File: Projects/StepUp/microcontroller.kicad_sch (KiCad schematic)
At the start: 31 parts, among them J1 USB_C_Receptacle_USB2.0_16P, J3 Conn_02x03_Odd_Even, J4 Conn_02x06_Odd_Even, SW1 PTS636SL43SMTRLFS, SW5 PTS636SL43SMTRLFS, U1 USBLC6-2SC6, U10 W25Q16JVUXIQ TR, U3 RP2040, Y1 ABM8-272-T3

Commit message: feat(v0.2): Rough layout begins
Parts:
- removed J4: Conn_02x06_Odd_Even, Connector_PinHeader_2.54mm:PinHeader_2x06_P2.54mm_Vertical, symbol Connector_Generic:Conn_02x06_Odd_Even
- removed SW5: PTS636SL43SMTRLFS, Snapeda:SW_PTS636S-J_CNK, symbol Snapeda_kicad:PTS636SL43SMTRLFS
- added SW2: PTS636SL43SMTRLFS, Snapeda:SW_PTS636S-J_CNK, symbol Snapeda_kicad:PTS636SL43SMTRLFS
- D1: Description_1 (none) -> DIODE GEN PURP 100V 150MA SOD123; Digi-Key_PN (none) -> 1N4148WTPMSCT-ND
- renumbered C15 to C14, J3 to J2, U10 to U1, U1 to U2
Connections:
- net GND: now also SW2.1
- net RUN: now also SW1.2
- net at D1.K: now also SW2.2; no longer SW1.2
- no-connect marks 2 -> 9
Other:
- note added: "Run - resets MCU USB_BOOT - hold this and toggle Run to enumerate as USB device for UF2 firmware upload NOTE: Buttons are SMD and usually hidden from user"
- note removed: "I2C_0/1 SPI_1 UART_0"
- note removed: "I2C_1"
- note removed: "Run - resets MCU USB_BOOT - hold this and toggle Run to enumerate as USB device for UF2 firmware upload"

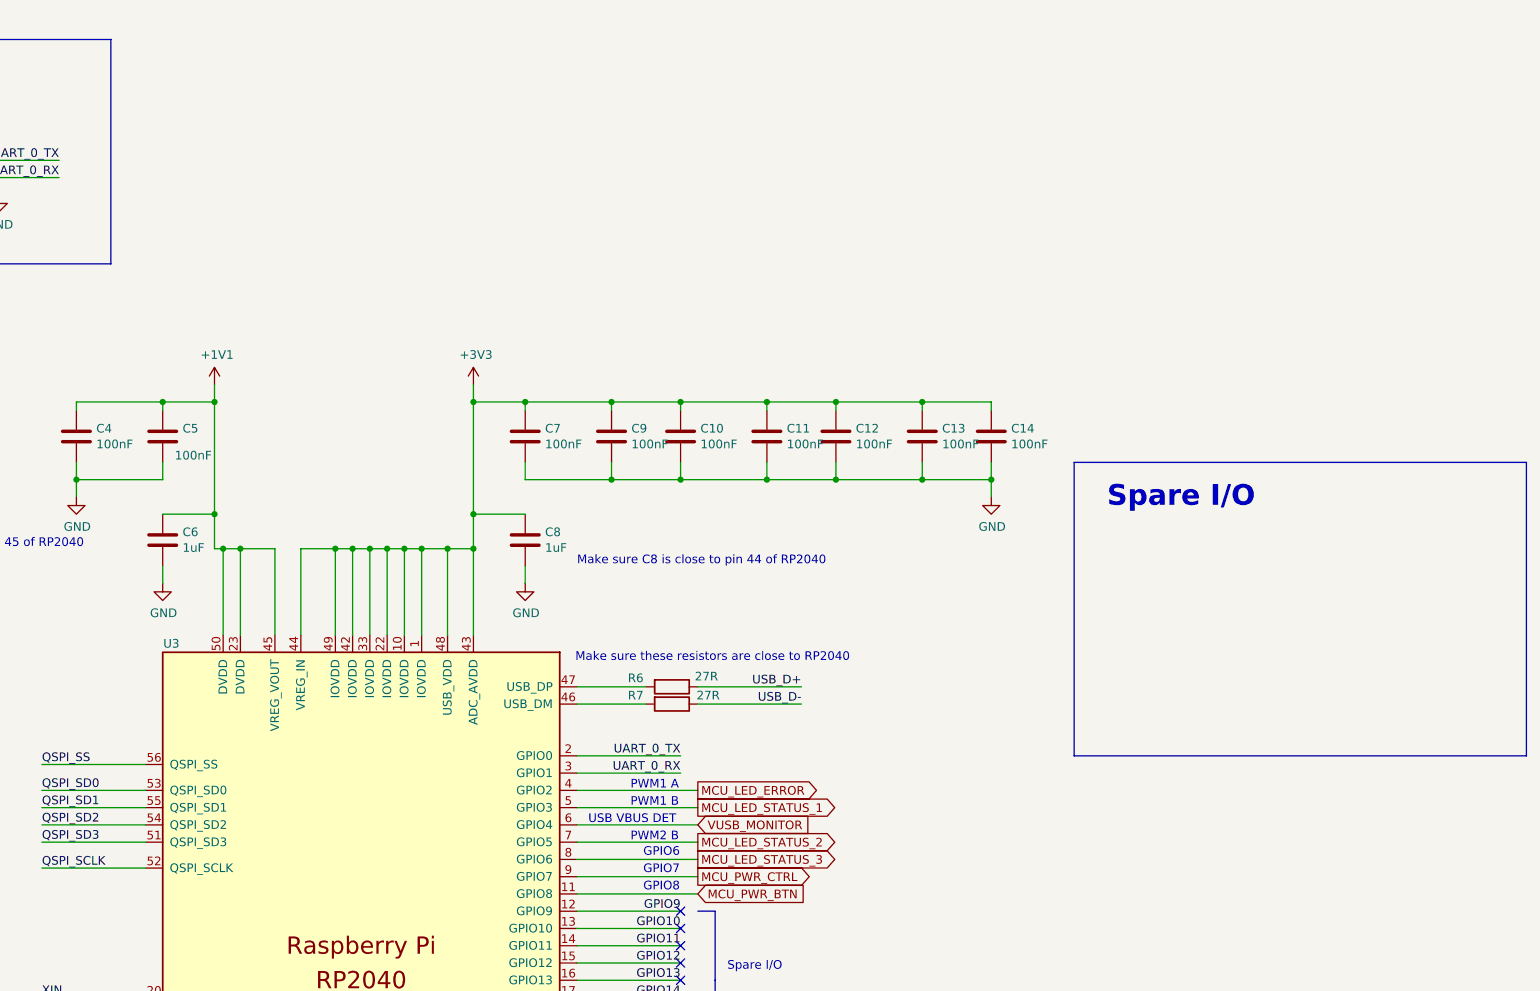
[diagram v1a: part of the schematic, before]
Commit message: feat(v0.2): Component layout from CAD
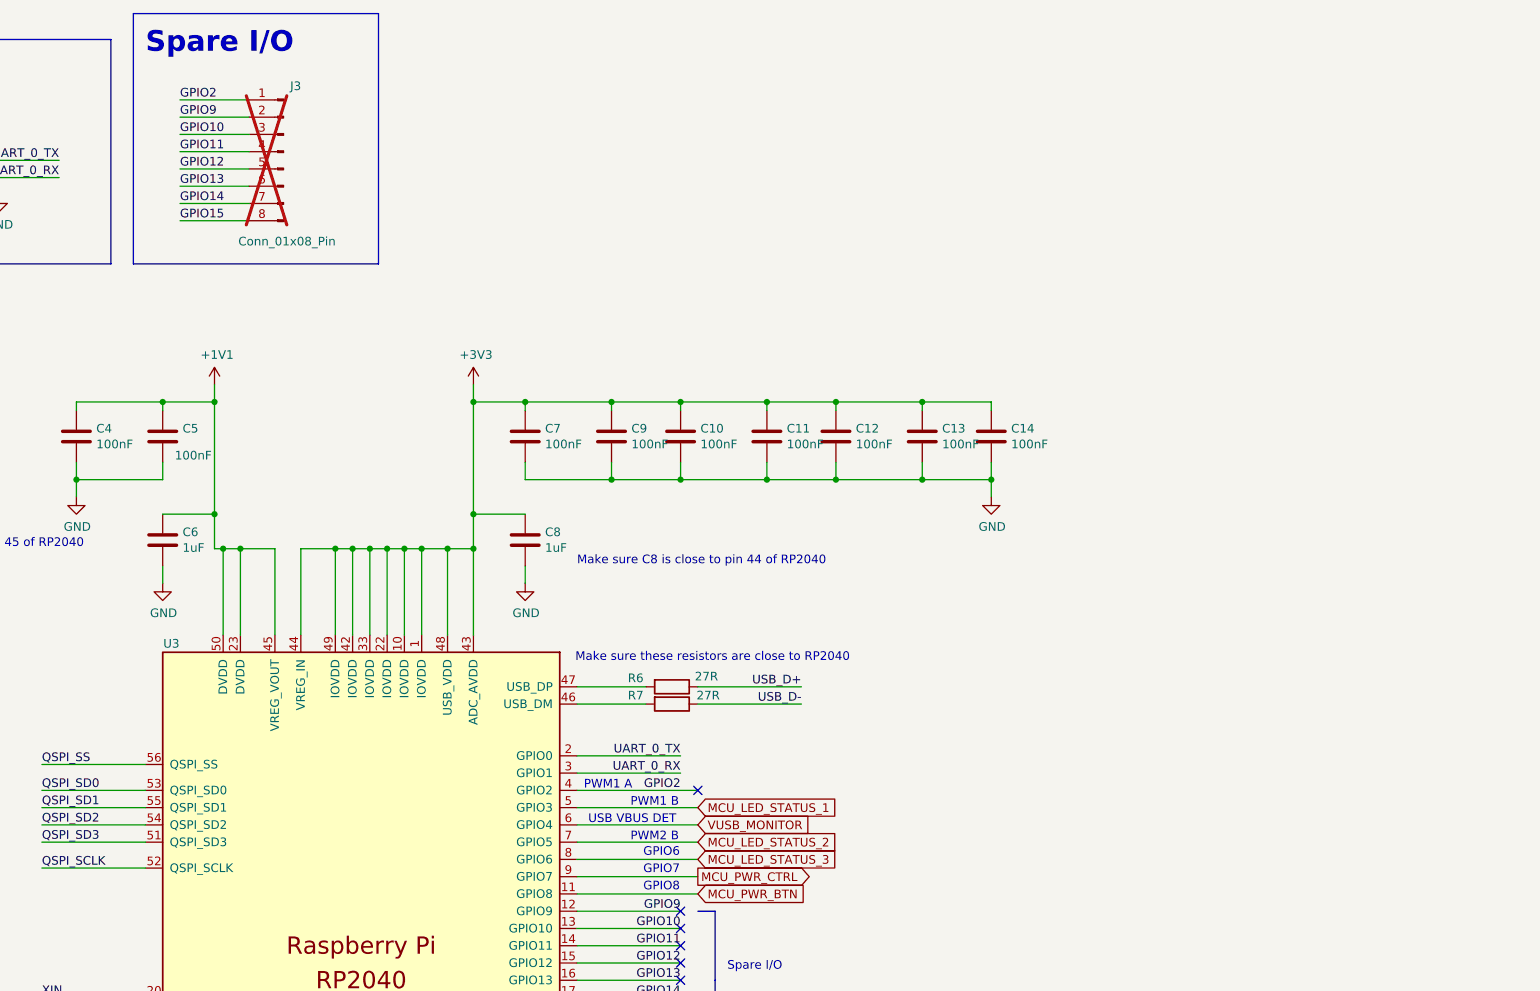
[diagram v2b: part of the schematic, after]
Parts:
- added J3: Conn_01x08_Pin, Connector_PinHeader_2.54mm:PinHeader_1x08_P2.54mm_Vertical, symbol Connector:Conn_01x08_Pin
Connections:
- net GPIO10: now also J3.3 (Pin_3)
- net GPIO11: now also J3.4 (Pin_4)
- net GPIO12: now also J3.5 (Pin_5)
- net GPIO13: now also J3.6 (Pin_6)
- net GPIO14: now also J3.7 (Pin_7)
- net GPIO15: now also J3.8 (Pin_8)
- net GPIO9: now also J3.2 (Pin_2)
- net MCU_LED_ERROR renamed GPIO2
- net GPIO2: now also J3.1 (Pin_1)
- no-connect marks 9 -> 10

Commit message: feat(v0.2): Release, PCBs ordered!
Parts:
- removed J3: Conn_01x08_Pin, Connector_PinHeader_2.54mm:PinHeader_1x08_P2.54mm_Vertical, symbol Connector:Conn_01x08_Pin
- added J5: Conn_01x09_Pin, Connector_PinHeader_2.54mm:PinHeader_1x09_P2.54mm_Vertical, symbol Connector:Conn_01x09_Pin
- J2: now fitted; now left out of the parts list
- SW1, SW2: value PTS636SL43SMTRLFS -> PTS636SP43SMTRL FS; MPN (none) -> PTS636SP43SMTR LFS; Manufacturer (none) -> C&K
- U1: MPN (none) -> W25Q16JVUXIQ TR; Manufacturer (none) -> Winbond Electronics
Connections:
- net GND: now also J5.1 (Pin_1)
- net GPIO10: now also J5.4 (Pin_4)
- net GPIO11: now also J5.5 (Pin_5)
- net GPIO12: now also J5.6 (Pin_6)
- net GPIO13: now also J5.7 (Pin_7)
- net GPIO14: now also J5.8 (Pin_8)
- net GPIO15: now also J5.9 (Pin_9)
- net GPIO2: now also J5.2 (Pin_2)
- net GPIO9: now also J5.3 (Pin_3)
- no-connect marks 10 -> 2

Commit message: feat(v0.3): Begin work on next rev
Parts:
- renumbered J5 to J2, J2 to J3
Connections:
- net MCU_LED_STATUS_1 renamed MCU_LED_RED
- net MCU_LED_STATUS_2 renamed MCU_LED_BLUE
- net MCU_LED_STATUS_3 renamed MCU_LED_GREEN

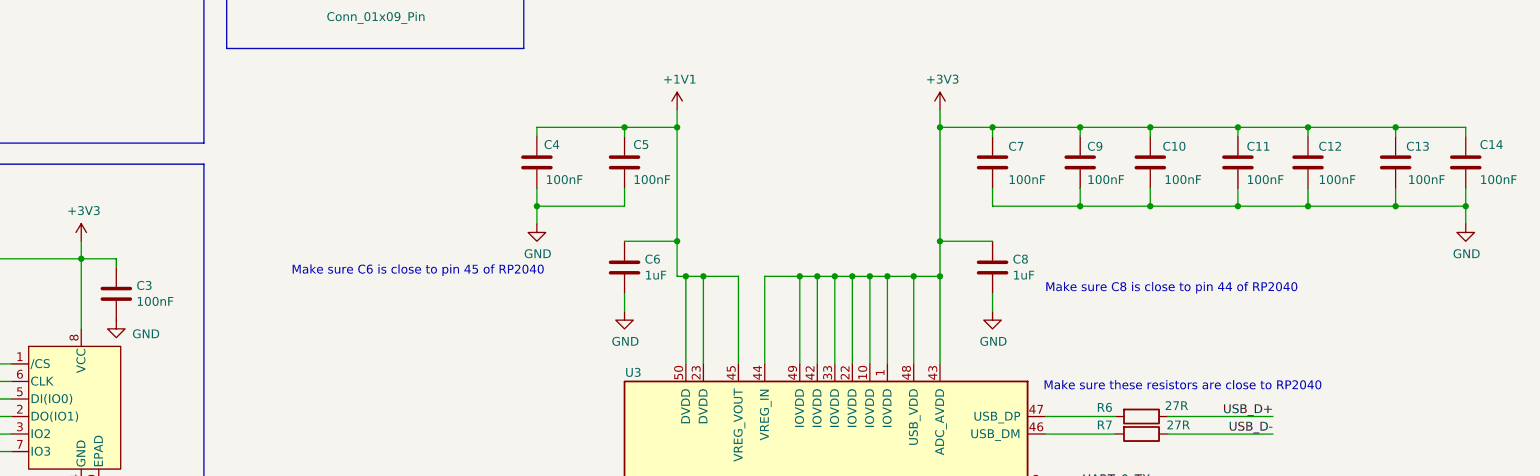
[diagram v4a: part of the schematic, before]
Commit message: feat(v0.3): Boost layout complete
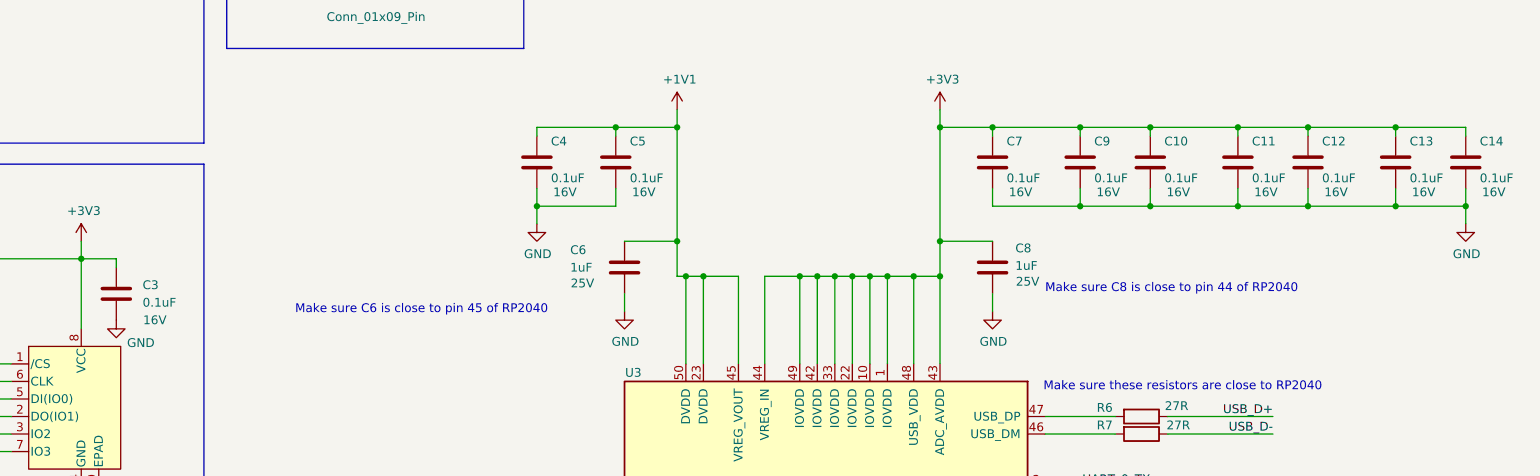
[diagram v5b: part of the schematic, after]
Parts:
- C10, C11, C12, C13, C14, C3, C4, C5, C7, C9: value 100nF -> 0.1uF; Dielectric X7R -> X5R; MPN CC0402KRX7R8BB104 -> GRM155R61C104KA88D; Manufacturer YAGEO -> Murata; Package 0402 -> 0402; Voltage 25V -> 16V
- C6, C8: footprint Capacitor_SMD:C_0402_1005Metric -> Capacitor_SMD:C_0603_1608Metric; Dielectric X5R -> X7R; MPN GRM155R61E105MA12D -> GRM188R71E105KA12D; Manufacturer Murata Electronics -> Murata; Package 0402 -> 0603; Tolerance 20% -> 10%

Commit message: feat(v0.3): Layout 90% complete
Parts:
- removed J2: Conn_01x09_Pin, Connector_PinHeader_2.54mm:PinHeader_1x09_P2.54mm_Vertical, symbol Connector:Conn_01x09_Pin
- removed SW1, SW2: PTS636SP43SMTRL FS, Snapeda:SW_PTS636S-J_CNK, symbol Snapeda_kicad:PTS636SL43SMTRLFS
- added J2: Conn_01x05_Pin, Connector_PinHeader_2.54mm:PinHeader_1x05_P2.54mm_Vertical, symbol Connector:Conn_01x05_Pin
- added J3: Conn_01x04_Pin, Connector_PinHeader_2.54mm:PinHeader_1x04_P2.54mm_Vertical, symbol Connector:Conn_01x04_Pin
- added SW1, SW2: 434153017835, Snapeda:434153017835_434153017835, symbol Snapeda:434153017835
- renumbered J3 to J4
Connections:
- net GND: now also J2.1 (Pin_1), SW1.1, SW1.3, SW2.1, SW2.3
- net GPIO10: now also J2.4 (Pin_4)
- net GPIO11: now also J2.5 (Pin_5)
- net GPIO12: now also J3.1 (Pin_1)
- net GPIO13: now also J3.2 (Pin_2)
- net GPIO14: now also J3.3 (Pin_3)
- net GPIO15: now also J3.4 (Pin_4)
- net GPIO2: now also J2.2 (Pin_2)
- net GPIO9: now also J2.3 (Pin_3)
- net RUN: now also SW1.2, SW1.4
- net at D1.K: now also SW2.2, SW2.4

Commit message: feat(v0.3): Files sent to PCBWay for build
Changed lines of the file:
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@@
+			"AAAAAAAAAAAAAAAAAAAAAAAAAAAAAAAAAAAAAAAAAAAAAAAAAAAAAAAAAAAAAAAAAAAAAAAAAAAA"
+			"AAAAAAAAAAAAAAAAAAAAAAAAAAAAAAAAAAAAAAAAAAAAAAAAAAAAAAAAAAAAAAAAAAAAAAAAAAAA"
+			"AAAAAAAAAAAAAAAAAAAAAAAAAAAAAAAAAAAAAAAAAAAAAAAAAAAAAAAAAAAAAAAAAAAAAAAAAAAA"
+			"AAAAAAAAAAAAAAAAAAAAAAAAAAAAAAAAAAAAAAAAAAAAAAAAAAAAAAAAAAAAAAAAAAAAAAAAAAAA"
+			"AAAAAAAAAAAAAAAAAAAAAAAAAAAAAAAAAAAAAAAAAAAAAAAAAAAAAAAAAAAAAAAAAAAAAAAAAAAA"
+			"AAAAAAAAAAAAAAAAAAAAAAAAAAAAAAAAAAAAAAAAAAAAAAAAAAAAAAAAAAAAAAAAAAAAAAAAAAAA"
+			"AAAAAAAAAAAAAAAAAAAAAAAAAAAAAAAAAAAAAAAAAAAAAAAAAAAAAAAAAAAAAAAAAAAAAAAAAAAA"
+			"AAAAAAAAAAAAAAAAAAAAAAAAAAAAAAAAAAAAAAAAAAAAAAAAAAAAAAAAAAAAAAAAAAAAAAAAAAAA"
+			"AAAAAAAAAAAAAAAAAAAAAAAAAAAAAAAAAAAAAAAAAAAAAAAAAAAAAAAAAAAAAAAAAAAAAAAAAAAA"
+			"AAAAAAAAAAAAAAAAAAAAAAAAAAAAAAAAAAAAAAAAAAAAAAAAAAAAAAAAAAAAAAAAAAAAAAAAAAAA"
+			"AAAAAAAAAAAAAAAAAAAAAAAAAAAAAAAAAAAAAAAAAAAAAAAAAAAAAAAAAAAAAAAAAAAAAAAAAAAA"
+			"AAAAAAAAAAAAAAAAAAAAAAAAAAAAAAAAAAAAAAAAAAAAAAAAAAAAAAAAAAAAAAAAAAAAAAAAAAAA"
+			"AAAAAAAAAAAAAAAAAAAAAAAAAAAAAAAAAAAAAAAAAAAAAAAAAAAAAAAAAAAAAAAAAAAAAAAAAAAA"
+			"AAAAAAAAAAAAAAAAAAAAAAAAAAAAAAAAAAAAAAAAAAAAAAAAAAAAAAAAAAAAAAAAAAAAAAAAAAAA"
+			"AAAAAAAAAAAAAAAAAAAAAAAAAAAAAAAAAAAAAAAAAAAAAAAAAAAAAAAAAAAAAAAAAAAAAAAAAAAA"
+			"AAAAAAAAAAAAAAAAAAAAAAAAAAAAAAAAAAAAAAAAAAAAAAAAAAAAAAAAAAAAAAAAAAAAAAAAAAAA"
+			"AAAAAAAAAAAAAAAAAAAAAAAAAAAAAAAAAAAAAAAAAAAAAAAAAAAAAAAAAAAAAAAAAAAAAAAAAAAA"
+			"AAAAAAAAAAAAAAAAAAAAAAAAAAAAAAAAAAAAAAAAAAAAAAAAAAAAAAAAAAAAAAAAAAAAAAAAAAAA"
 			"AAAAAAAAAAAAAAAAAAAAAAAAAAAAAAAAAAAAAAAAAAAAAAAAAAAAAAAAAAAAAAAAAAAAAAAAAAAA"
 			"AAAAAAAAAAAAAAAAAAAAAAAAAAAAAAAAAAAAAAAAAAAAAAAAAAAAAAAAAAAAAAAAAAAAAAAAAAAA"
@@
 		)
 	)
+	(label "~{USB_BOOT}"
+		(at 43.18 114.3 0)
+		(effects
+			(font
+				(size 1.27 1.27)
+			)
+			(justify left bottom)
+		)
+	)
 	(label "UART_0_RX"
 		(at 217.17 48.26 180)
@@
 		)
 	)
+	(label "~{USB_BOOT}"
+		(at 90.17 66.04 180)
+		(effects
+			(font
+				(size 1.27 1.27)
+			)
+			(justify right bottom)
+		)
+	)
 	(label "GPIO12"
 		(at 140.97 57.15 0)
@@
 		)
 	)
-	(label "~{USB_BOOT}"
-		(at 45.72 114.3 0)
-		(effects
-			(font
-				(size 1.27 1.27)
-			)
-			(justify left bottom)
-		)
-	)
 	(label "GPIO15"
 		(at 140.97 64.77 0)
@@
 		(effects
 			(font
-				(size 1.27 1.27)
-			)
-			(justify left bottom)
-		)
-	)
-	(label "~{USB_BOOT}"
-		(at 80.01 66.04 0)
-		(effects
-			(font

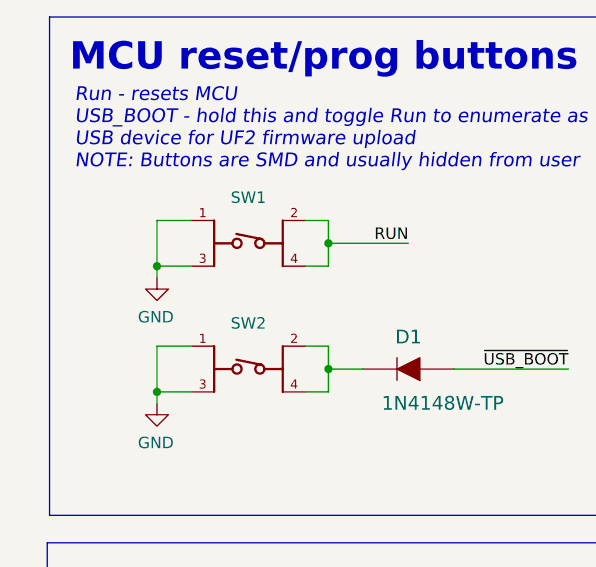
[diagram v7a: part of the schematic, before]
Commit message: feat(v0.3): Minor updates for PCBWay order
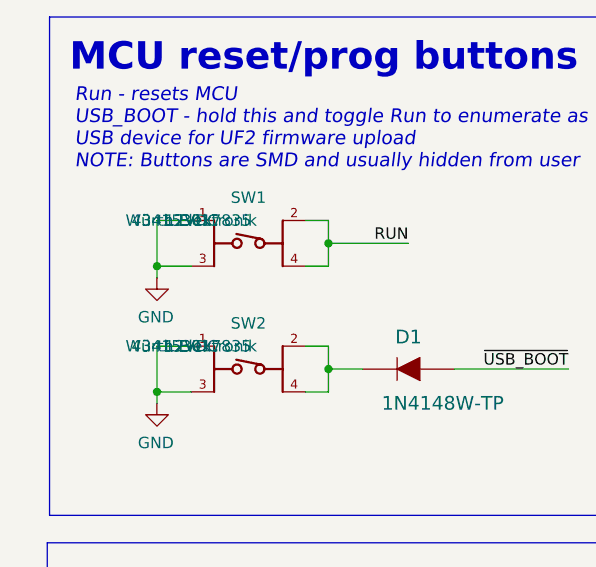
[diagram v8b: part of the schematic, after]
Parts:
- J2, J3: now left out of the parts list
- SW1, SW2: MPN (none) -> 434153017835; Manufacturer (none) -> Würth Elektronik; Voltage (none) -> 12VDC
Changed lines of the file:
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@@
 			"AAAAAAAAAAAAAAAAAAAAAAAAAAAAAAAAAAAAAAAAAAAAAAAAAAAAAAAAAAAAAAAAAAAAAAAAAAAA"
 			"AAAAAAAAAAAAAAAAAAAAAAAAAAAAAAAAAAAAAAAAAAAAAAAAAAAAAAAAAAAAAAAAAAAAAAAAAAAA"
+			"AAAAAAAAAAAAAAAAAAAAAAAAAAAAAAAAAAAAAAAAAAAAAAAAAAAAAAAAAAAAAAAAAAAAAAAAAAAA"
+			"AAAAAAAAAAAAAAAAAAAAAAAAAAAAAAAAAAAAAAAAAAAAAAAAAAAAAAAAAAAAAAAAAAAAAAAAAAAA"
+			"AAAAAAAAAAAAAAAAAAAAAAAAAAAAAAAAAAAAAAAAAAAAAAAAAAAAAAAAAAAAAAAAAAAAAAAAAAAA"
+			"AAAAAAAAAAAAAAAAAAAAAAAAAAAAAAAAAAAAAAAAAAAAAAAAAAAAAAAAAAAAAAAAAAAAAAAAAAAA"
+			"AAAAAAAAAAAAAAAAAAAAAAAAAAAAAAAAAAAAAAAAAAAAAAAAAAAAAAAAAAAAAAAAAAAAAAAAAAAA"
+			"AAAAAAAAAAAAAAAAAAAAAAAAAAAAAAAAAAAAAAAAAAAAAAAAAAAAAAAAAAAAAAAAAAAAAAAAAAAA"
+			"AAAAAAAAAAAAAAAAAAAAAAAAAAAAAAAAAAAAAAAAAAAAAAAAAAAAAAAAAAAAAAAAAAAAAAAAAAAA"
+			"AAAAAAAAAAAAAAAAAAAAAAAAAAAAAAAAAAAAAAAAAAAAAAAAAAAAAAAAAAAAAAAAAAAAAAAAAAAA"
+			"AAAAAAAAAAAAAAAAAAAAAAAAAAAAAAAAAAAAAAAAAAAAAAAAAAAAAAAAAAAAAAAAAAAAAAAAAAAA"
+			"AAAAAAAAAAAAAAAAAAAAAAAAAAAAAAAAAAAAAAAAAAAAAAAAAAAAAAAAAAAAAAAAAAAAAAAAAAAA"
+			"AAAAAAAAAAAAAAAAAAAAAAAAAAAAAAAAAAAAAAAAAAAAAAAAAAAAAAAAAAAAAAAAAAAAAAAAAAAA"
+			"AAAAAAAAAAAAAAAAAAAAAAAAAAAAAAAAAAAAAAAAAAAAAAAAAAAAAAAAAAAAAAAAAAAAAAAAAAAA"
+			"AAAAAAAAAAAAAAAAAAAAAAAAAAAAAAAAAAAAAAAAAAAAAAAAAAAAAAAAAAAAAAAAAAAAAAAAAAAA"
+			"AAAAAAAAAAAAAAAAAAAAAAAAAAAAAAAAAAAAAAAAAAAAAAAAAAAAAAAAAAAAAAAAAAAAAAAAAAAA"
+			"AAAAAAAAAAAAAAAAAAAAAAAAAAAAAAAAAAAAAAAAAAAAAAAAAAAAAAAAAAAAAAAAAAAAAAAAAAAA"
+			"AAAAAAAAAAAAAAAAAAAAAAAAAAAAAAAAAAAAAAAAAAAAAAAAAAAAAAAAAAAAAAAAAAAAAAAAAAAA"
+			"AAAAAAAAAAAAAAAAAAAAAAAAAAAAAAAAAAAAAAAAAAAAAAAAAAAAAAAAAAAAAAAAAAAAAAAAAAAA"
+			"AAAAAAAAAAAAAAAAAAAAAAAAAAAAAAAAAAAAAAAAAAAAAAAAAAAAAAAAAAAAAAAAAAAAAAAAAAAA"
 			"AAAAAA=="
 		)
@@
 		(unit 1)
 		(exclude_from_sim no)
-		(in_bom yes)
+		(in_bom no)
 		(on_board yes)
 		(dnp no)
@@
 			)
 		)
+		(property "MPN" "434153017835"
+			(at 48.26 63.5 0)
+			(effects
+				(font
+					(size 1.27 1.27)
+				)
+			)
+		)
+		(property "Manufacturer" "Würth Elektronik"
+			(at 48.26 63.5 0)
+			(effects
+				(font
+					(size 1.27 1.27)
+				)
+			)
+		)
+		(property "Voltage" "12VDC"
+			(at 48.26 63.5 0)
+			(effects
+				(font
+					(size 1.27 1.27)
+				)
+			)
+		)
 		(pin "3"
 		)
@@
 			)
 		)
+		(property "MPN" "434153017835"
+			(at 48.26 49.53 0)
+			(effects
+				(font
+					(size 1.27 1.27)
+				)
+			)
+		)
+		(property "Manufacturer" "Würth Elektronik"
+			(at 48.26 49.53 0)
+			(effects
+				(font
+					(size 1.27 1.27)
+				)
+			)
+		)
+		(property "Voltage" "12VDC"
+			(at 48.26 49.53 0)
+			(effects
+				(font
+					(size 1.27 1.27)
+				)
+			)
+		)
 		(pin "3"
 		)
@@
 		(unit 1)
 		(exclude_from_sim no)
-		(in_bom yes)
+		(in_bom no)
 		(on_board yes)
 		(dnp no)
